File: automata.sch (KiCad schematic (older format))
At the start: 124 parts, among them J1 Barrel_Jack, J2 LCD, J3 ICSP, J4 SERIAL, Q1 2N2907, Q2 IRF5305PBF, SW1 INPUT_SEL, SW2 SW_DIP_x08, SW3 Reset, U1 74HC164, U10 TLC555-Timer, U11 4040, U12 74HC11, U13 4024, U14 74HC139, U15 74HC04, U16 4053, U17 74HC164, U18 74HC164, U19 74HC164, U2 4077, U20 74HC164, U21 74HC164, U22 74HC164, U23 74HC164, U24 74HC164, U25 4013, U26 ATmega328-PU, U27 MCP1700-3302E_TO92, U3 74HC164, U4 74HC164, U5 74HC373, U6 74HC373, U7 74HC165, U8 4512, U9 TLC555-Timer, X1 16MHz

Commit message: LDO change to streamline the inventory
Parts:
- removed C29, C30: 1uF, Capacitor_THT:C_Disc_D5.1mm_W3.2mm_P5.00mm, symbol Device:C
- removed U27: MCP1700-3302E_TO92, Package_TO_SOT_THT:TO-92_Inline, symbol Regulator_Linear:MCP1700-3302E_TO92
- added C29, C30: 10uF, Capacitor_THT:CP_Radial_D5.0mm_P2.00mm, symbol Device:CP
- added U27: HT7333, Package_TO_SOT_THT:TO-92_Inline, symbol InGarage_Regulator_Linear:HT73xx
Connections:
- net +3V3: now also C30.1, U27.3 (OUT)
- net +5V: now also C29.1, U27.2 (IN)
- net GNDREF: now also C29.2, C30.2, U27.1 (GND)
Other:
- note added: "Alternate parts:\nMCP1700-3302E\n"
- note added: "Alternate parts:\nSS-12D02-VG4"
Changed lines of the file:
@@
 	1    0    0    -1
 $EndComp
-$Comp
-L Regulator_Linear:MCP1700-3302E_TO92 U27
-U 1 1 604FE86F
-P 18800 1050
-F 0 "U27" H 18800 808 50  0000 C CNN
-F 1 "MCP1700-3302E_TO92" H 18800 899 50  0000 C CNN
-F 2 "Package_TO_SOT_THT:TO-92_Inline" H 18800 850 50  0001 C CIN
-F 3 "http://ww1.microchip.com/downloads/en/DeviceDoc/20001826D.pdf" H 18800 1050 50  0001 C CNN
-	1    18800 1050
-	1    0    0    1
-$EndComp
-$Comp
-L Device:C C29
-U 1 1 605B50D5
-P 18250 1200
-F 0 "C29" H 18365 1246 50  0000 L CNN
-F 1 "1uF" H 18365 1155 50  0000 L CNN
-F 2 "Capacitor_THT:C_Disc_D5.1mm_W3.2mm_P5.00mm" H 18288 1050 50  0001 C CNN
-F 3 "~" H 18250 1200 50  0001 C CNN
-	1    18250 1200
-	1    0    0    -1
-$EndComp
-$Comp
-L Device:C C30
-U 1 1 605B597E
-P 19350 1200
-F 0 "C30" H 19465 1246 50  0000 L CNN
-F 1 "1uF" H 19465 1155 50  0000 L CNN
-F 2 "Capacitor_THT:C_Disc_D5.1mm_W3.2mm_P5.00mm" H 19388 1050 50  0001 C CNN
-F 3 "~" H 19350 1200 50  0001 C CNN
-	1    19350 1200
-	1    0    0    -1
-$EndComp
-Wire Wire Line
-	18250 1050 18500 1050
 Connection ~ 19350 1050
 $Comp
@@
 Wire Wire Line
 	17250 1050 17800 1050
-Wire Wire Line
-	17800 1050 18250 1050
 Connection ~ 17800 1050
-Connection ~ 18250 1050
 $Comp
 L Device:LED D7
@@
 Wire Wire Line
 	4350 14200 4350 14550
+$Comp
+L InGarage_Regulator_Linear:HT73xx U27
+U 1 1 5F6E78EE
+P 18800 1050
+F 0 "U27" H 18800 1292 50  0000 C CNN
+F 1 "HT7333" H 18800 1201 50  0000 C CNN
+F 2 "Package_TO_SOT_THT:TO-92_Inline" H 18800 1200 50  0001 C CNN
+F 3 "" H 18800 1200 50  0001 C CNN
+	1    18800 1050
+	1    0    0    -1
+$EndComp
+Text Notes 18500 2000 0    50   ~ 0
+Alternate parts:\nMCP1700-3302E\n
+$Comp
+L Device:CP C30
+U 1 1 5F9019FE
+P 19350 1200
+F 0 "C30" H 19468 1246 50  0000 L CNN
+F 1 "10uF" H 19468 1155 50  0000 L CNN
+F 2 "Capacitor_THT:CP_Radial_D5.0mm_P2.00mm" H 19388 1050 50  0001 C CNN
+F 3 "~" H 19350 1200 50  0001 C CNN
+	1    19350 1200
+	1    0    0    -1
+$EndComp
+Wire Wire Line
+	17800 1050 18250 1050
+$Comp
+L Device:CP C29
+U 1 1 5F906BE4
+P 18250 1200
+F 0 "C29" H 18368 1246 50  0000 L CNN
+F 1 "10uF" H 18368 1155 50  0000 L CNN
+F 2 "Capacitor_THT:CP_Radial_D5.0mm_P2.00mm" H 18288 1050 50  0001 C CNN
+F 3 "~" H 18250 1200 50  0001 C CNN
+	1    18250 1200
+	1    0    0    -1
+$EndComp
+Connection ~ 18250 1050
+Wire Wire Line
+	18250 1050 18500 1050
 Wire Bus Line
 	8600 1450 8600 3950
@@
 Wire Bus Line
 	8600 3950 8600 5300
+Text Notes 1750 3650 0    50   ~ 0
+Alternate parts:\nSS-12D02-VG4
 $EndSCHEMATC

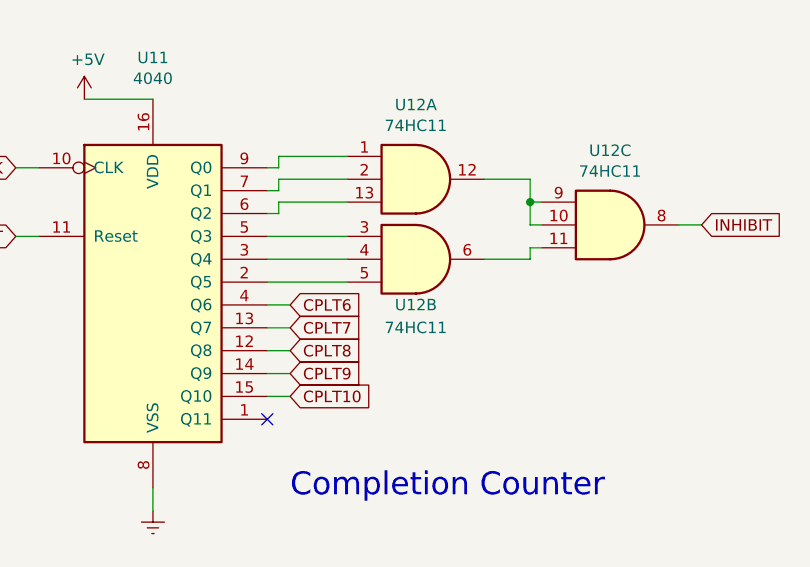
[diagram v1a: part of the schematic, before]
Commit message: reroute standard pcb
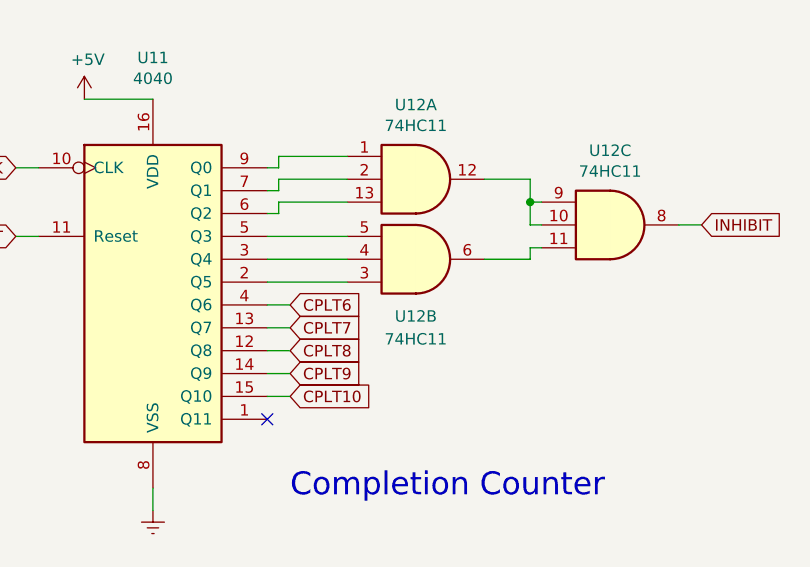
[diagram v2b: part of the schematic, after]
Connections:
- net at U12.3: now also U11.2 (Q5); no longer U11.5 (Q3)
- net at U12.5: now also U11.5 (Q3); no longer U11.2 (Q5)
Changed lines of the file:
@@
 Sheet 1 1
 Title "Elementary Cellular Automata Generator [Standard]"
-Date "2020-08-26"
-Rev "3"
+Date "2020-10-03"
+Rev "4"
 Comp "Sleepy Pony Labs"
-Comment1 "Rev.3 : Inprovements from rev 2"
+Comment1 "Rev.4 : Routing Improvement"
 Comment2 "Verified working"
 Comment3 ""
@@
 U 2 1 5DCAF89B
 P 15350 8250
-F 0 "U12" H 15350 8050 50  0000 C CNN
-F 1 "74HC11" H 15350 7950 50  0000 C CNN
+F 0 "U12" H 15350 8500 50  0000 C CNN
+F 1 "74HC11" H 15350 8600 50  0000 C CNN
 F 2 "Package_DIP:DIP-14_W7.62mm_Socket" H 15350 8250 50  0001 C CNN
 F 3 "" H 15350 8250 50  0001 C CNN
 	2    15350 8250
-	1    0    0    -1
+	1    0    0    1
 $EndComp
 NoConn ~ 14700 8950
@@
 Wire Wire Line
 	18250 1050 18500 1050
+Text Notes 1750 3650 0    50   ~ 0
+Alternate parts:\nSS-12D02-VG4
 Wire Bus Line
 	8600 1450 8600 3950
@@
 Wire Bus Line
 	8600 3950 8600 5300
-Text Notes 1750 3650 0    50   ~ 0
-Alternate parts:\nSS-12D02-VG4
 $EndSCHEMATC
